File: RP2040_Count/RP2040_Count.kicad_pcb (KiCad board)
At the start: 2 copper layers, 59 x 29.5 mm, 18 parts, among them J2 String1, J3 OLED, SW1 Test, U1 74AHCT1G125, U3 AMS1117-5.0, U4 INA219BxD, U5 RP2040-Tiny

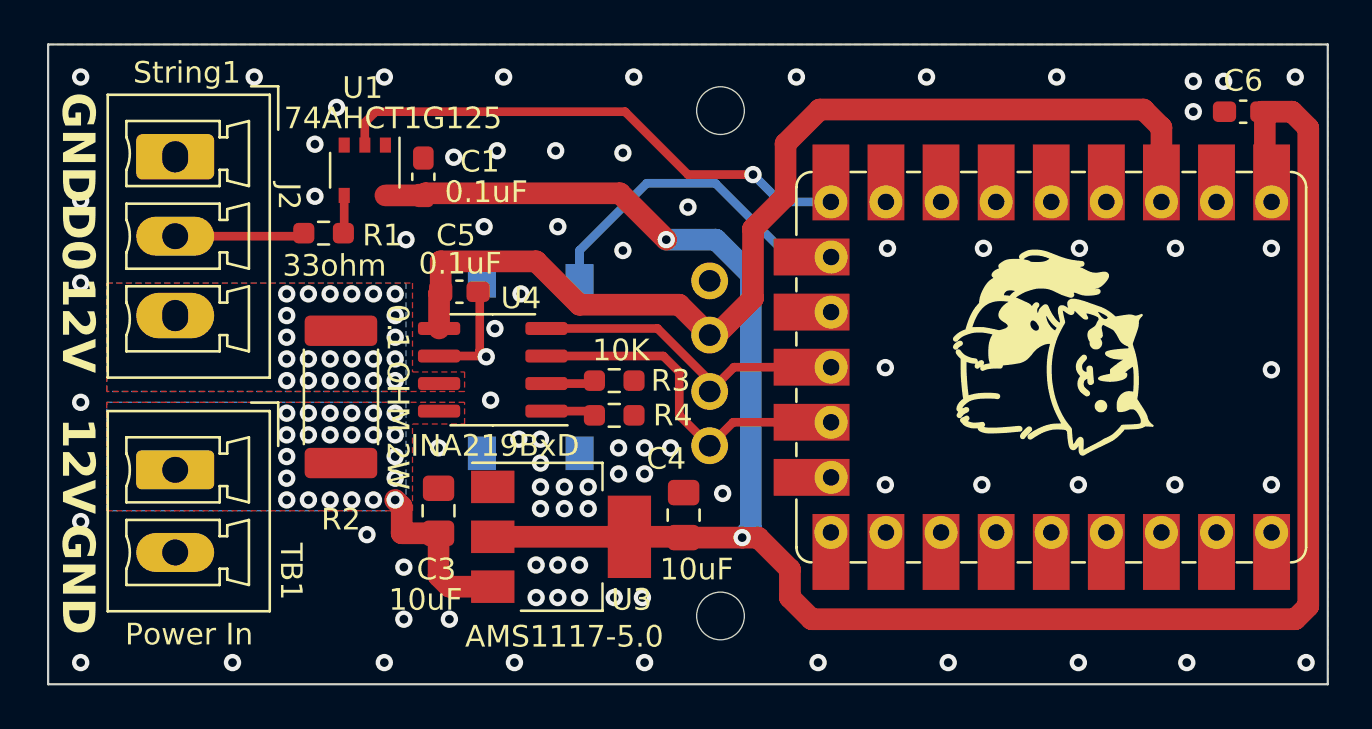
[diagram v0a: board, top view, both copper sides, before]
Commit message: add plug in 3 to 4 adapter
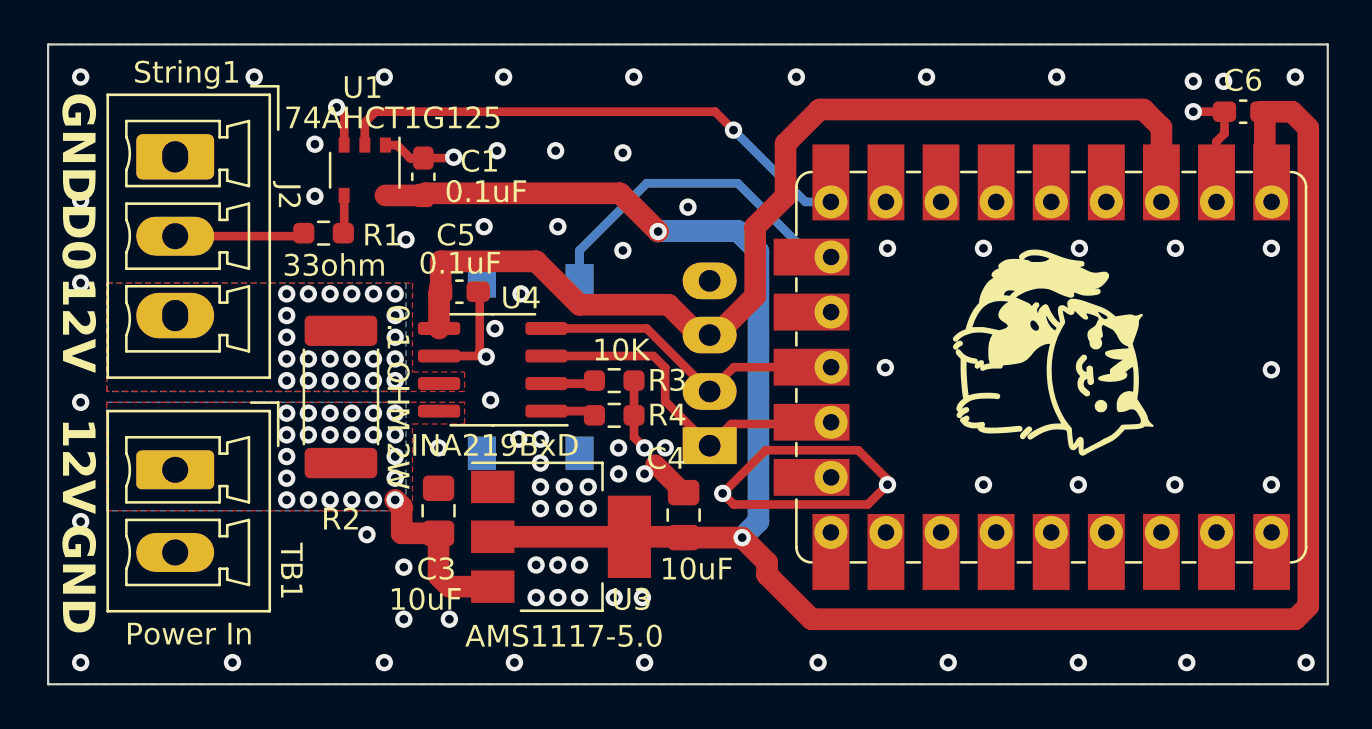
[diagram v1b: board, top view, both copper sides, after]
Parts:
- J3: footprint Scotts:OLED-SSD1306-128X64-I2C-THT_2HOLE -> Scotts:OLED-SSD1306-128X64-I2C-THT_SCOTT2
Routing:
- net GND: track 5.34 -> 39.7 mm
- net +5V: track 99.8 -> 100.5 mm
